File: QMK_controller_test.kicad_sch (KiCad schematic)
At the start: 14 parts, among them J1 USB_A, J3 BOOT0_HI_JMP, U1 STM32F042G6Ux, U2 XC6206PxxxMR

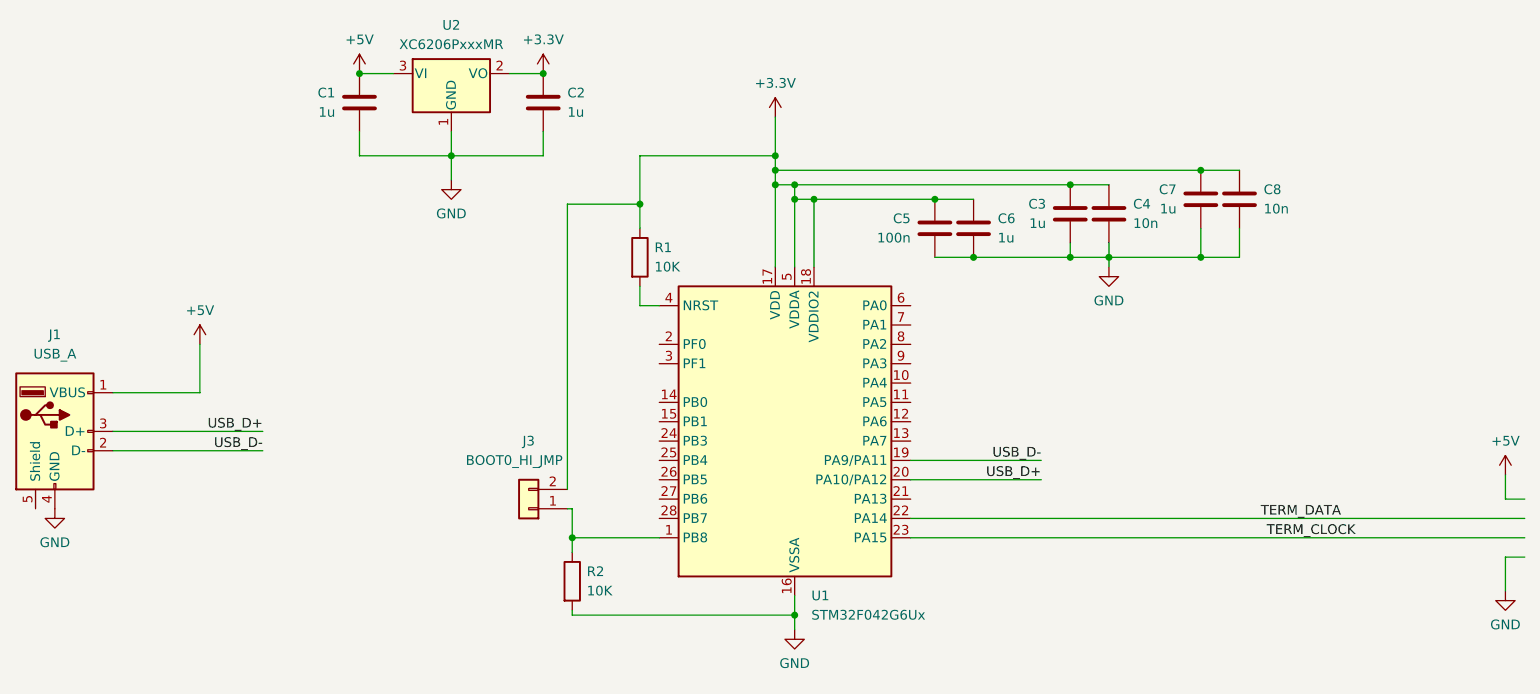
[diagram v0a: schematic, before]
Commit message: V0.2 - Fixed broken DIN 5 pinout. Fixed SWD conflict pinout (PB3 - DATA, PA15 - CLOCK). Also added SWD testpoints.
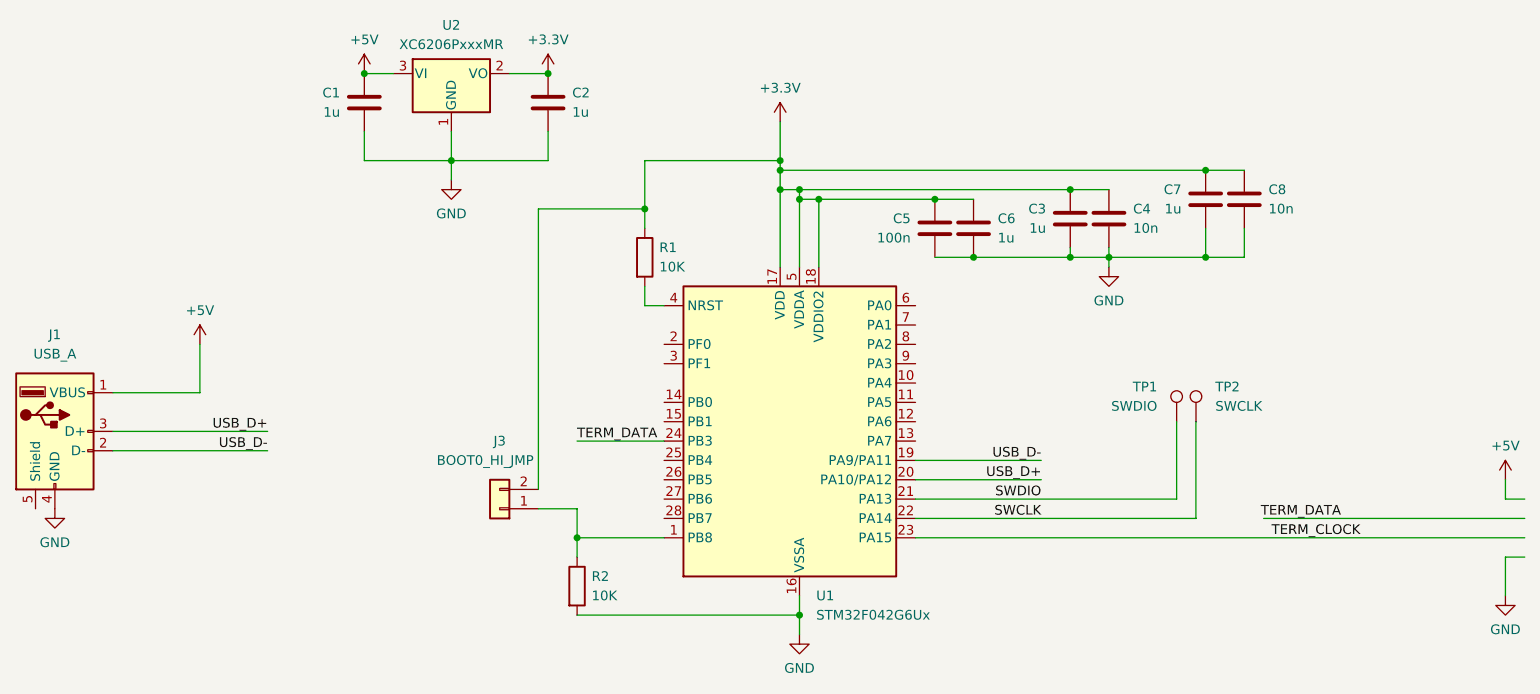
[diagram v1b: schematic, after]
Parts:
- added TP1: SWDIO, TestPoint:TestPoint_Pad_D1.0mm, symbol Connector:TestPoint
- added TP2: SWCLK, TestPoint:TestPoint_Pad_D1.0mm, symbol Connector:TestPoint
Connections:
- net TERM_DATA: now also U1.24 (PB3); no longer U1.22 (PA14)
- net SWDIO: now reaches U1.21 (PA13)
- net SWDIO: now also TP1.1
- new net SWCLK: TP2.1, U1.22 (PA14)
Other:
- moved on the sheet: C1, C2, C3, C4, C7, C8, J3, R1, R2, U1
